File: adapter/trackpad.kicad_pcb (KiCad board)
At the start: 2 copper layers, 41.9 x 19.7 mm, 15 parts, among them J1 J1, U1 Elite-C-nf, U2 ProMicro, U3 U3, U4 NCP1117-2.85_SOT223

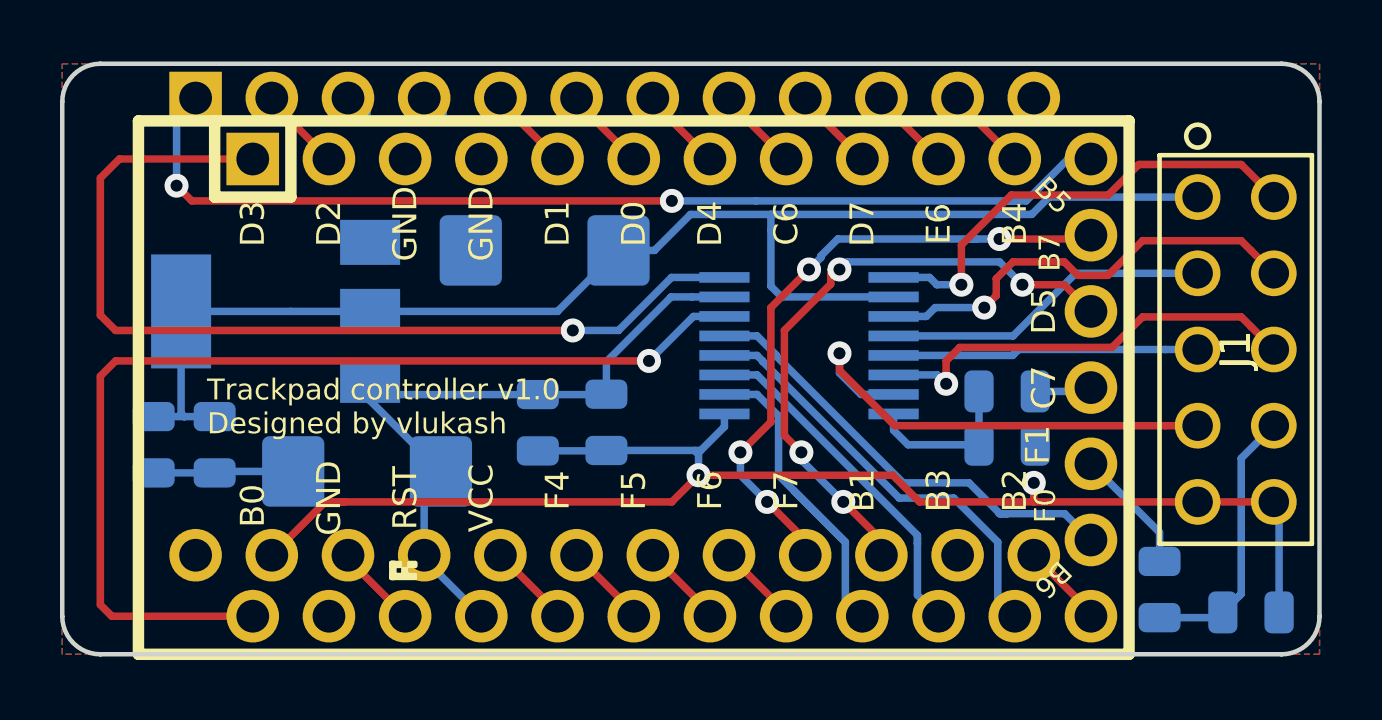
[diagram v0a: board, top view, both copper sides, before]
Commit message: Update PCB length so it doesn't block USB-C connector.
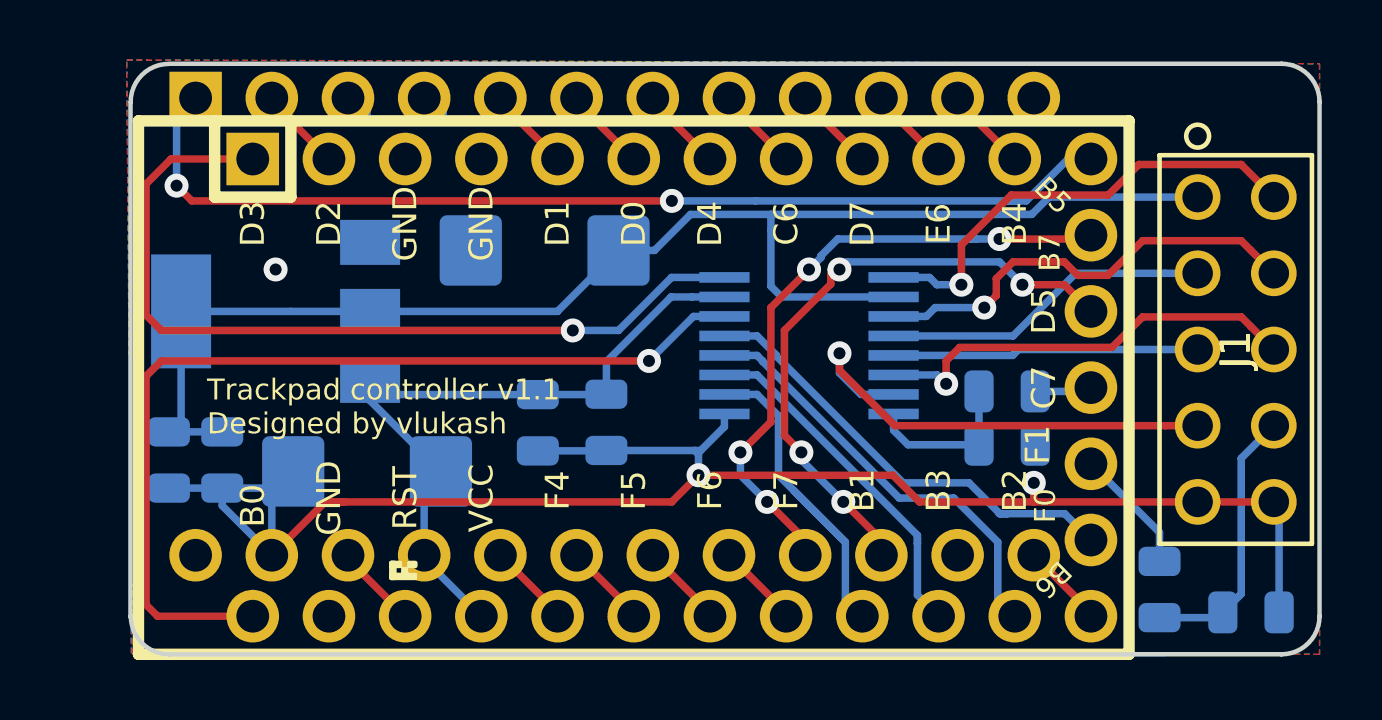
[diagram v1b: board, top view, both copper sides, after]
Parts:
- moved C5 0.72 mm to (98.8, 83.1)
- moved C6 0.57 mm to (100.6, 83.1)
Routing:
- net GND: track 55.8 -> 61.5 mm, vias 2 -> 3
- net TP_MOTION: track 31.7 -> 28.5 mm
- net TP_CS: track 35.9 -> 32.9 mm
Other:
- board size 41.9 x 19.7 mm -> 39.6 x 19.7 mm
- board text added: "Trackpad controller v1.1 Designed by vlukash"
- board text removed: "Trackpad controller v1.0 Designed by vlukash"
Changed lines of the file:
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@@
     (thickness 1.6)
     (drawings 9)
-    (tracks 268)
+    (tracks 272)
     (zones 0)
     (modules 15)
@@
     (title "Adapter PCB")
     (date 2019-01-16)
-    (rev 1.0)
+    (rev 1.1)
     (company vlukash)
   )
@@
     (42 Eco1.User user hide)
     (43 Eco2.User user hide)
-    (44 Edge.Cuts user hide)
+    (44 Edge.Cuts user)
     (45 Margin user hide)
     (46 B.CrtYd user hide)
@@
     (pcbplotparams
       (layerselection 0x010fc_ffffffff)
-      (usegerberextensions false)
+      (usegerberextensions true)
       (usegerberattributes false)
       (usegerberadvancedattributes false)
@@
       (drillshape 0)
       (scaleselection 1)
-      (outputdirectory "../plot/"))
+      (outputdirectory "../plot1/"))
   )
   (net 0 "")
@@
   )
   (module Capacitor_SMD:C_0805_2012Metric (layer B.Cu)
-    (at 98.298 82.55 270)
+    (at 98.806 83.058 270)
     (descr "Capacitor SMD 0805 (2012 Metric), square (rectangular) end terminal, IPC_7351 nominal, (Body size source: https://docs.google.com/spreadsheets/d/1BsfQQcO9C6DZCsRaXUlFlo91Tg2WpOkGARC1WS5S8t0/edit?usp=sharing), generated with kicad-footprint-generator")
     (tags capacitor)
@@
   )
   (module Capacitor_SMD:C_0805_2012Metric (layer B.Cu)
-    (at 100.33 82.55 270)
+    (at 100.584 83.058 270)
     (descr "Capacitor SMD 0805 (2012 Metric), square (rectangular) end terminal, IPC_7351 nominal, (Body size source: https://docs.google.com/spreadsheets/d/1BsfQQcO9C6DZCsRaXUlFlo91Tg2WpOkGARC1WS5S8t0/edit?usp=sharing), generated with kicad-footprint-generator")
     (tags capacitor)
@@
     )
   )
-  (gr_text "Trackpad controller v1.0\nDesigned by vlukash" (at 100.076 81.28) (layer F.SilkS)
+  (gr_text "Trackpad controller v1.1\nDesigned by vlukash" (at 100.076 81.28) (layer F.SilkS)
     (effects (font (size 0.7 0.7) (thickness 0.175)) (justify left))
   )
   (gr_arc (start 135.89 71.12) (end 137.16 71.12) (angle -90) (layer Edge.Cuts) (width 0.15))
   (gr_arc (start 135.89 88.265) (end 135.89 89.535) (angle -90) (layer Edge.Cuts) (width 0.15))
-  (gr_arc (start 96.52 88.265) (end 95.25 88.265) (angle -90) (layer Edge.Cuts) (width 0.15))
-  (gr_arc (start 96.52 71.12) (end 96.52 69.85) (angle -90) (layer Edge.Cuts) (width 0.15))
-  (gr_line (start 95.25 88.265) (end 95.25 71.12) (layer Edge.Cuts) (width 0.15))
-  (gr_line (start 135.89 89.535) (end 96.52 89.535) (layer Edge.Cuts) (width 0.15))
+  (gr_arc (start 98.806 88.265) (end 97.536 88.265) (angle -90) (layer Edge.Cuts) (width 0.15))
+  (gr_arc (start 98.8 71.125) (end 98.8 69.855) (angle -90) (layer Edge.Cuts) (width 0.15))
+  (gr_line (start 97.525 88.295) (end 97.525 71.15) (layer Edge.Cuts) (width 0.15))
+  (gr_line (start 135.89 89.535) (end 98.82 89.54) (layer Edge.Cuts) (width 0.15))
   (gr_line (start 137.16 71.12) (end 137.16 88.265) (layer Edge.Cuts) (width 0.15))
-  (gr_line (start 96.52 69.85) (end 135.89 69.85) (layer Edge.Cuts) (width 0.15))
+  (gr_line (start 98.83 69.85) (end 135.89 69.85) (layer Edge.Cuts) (width 0.15))
   (segment (start 107.95 71.755) (end 107.95 70.993) (width 0.25) (layer B.Cu) (net 1))
   (segment (start 107.95 70.993) (end 106.710725 70.993) (width 0.25) (layer B.Cu) (net 1))
   (segment (start 105.41 71.755) (end 105.41 70.993) (width 0.25) (layer B.Cu) (net 1))
   (segment (start 105.016299 71.386701) (end 105.41 70.993) (width 0.25) (layer B.Cu) (net 1))
-  (segment (start 100.3785 83.439) (end 100.33 83.4875) (width 0.25) (layer B.Cu) (net 1))
-  (segment (start 102.9475 83.439) (end 100.3785 83.439) (width 0.25) (layer B.Cu) (net 1))
-  (segment (start 100.33 83.4875) (end 98.298 83.4875) (width 0.25) (layer B.Cu) (net 1))
   (segment (start 104.013 84.455) (end 102.235 86.233) (width 0.25) (layer F.Cu) (net 1))
   (segment (start 104.648 84.455) (end 104.013 84.455) (width 0.25) (layer F.Cu) (net 1))
@@
   (segment (start 116.332 82.740969) (end 116.53243 82.740969) (width 0.25) (layer B.Cu) (net 1))
   (segment (start 113.388145 82.740969) (end 116.332 82.740969) (width 0.25) (layer B.Cu) (net 1))
+  (segment (start 100.584 83.9955) (end 98.806 83.9955) (width 0.25) (layer B.Cu) (net 1))
+  (segment (start 102.391 83.9955) (end 102.9475 83.439) (width 0.25) (layer B.Cu) (net 1))
+  (segment (start 100.584 83.9955) (end 102.391 83.9955) (width 0.25) (layer B.Cu) (net 1))
+  (segment (start 100.584 84.582) (end 100.584 83.9955) (width 0.25) (layer B.Cu) (net 1))
+  (segment (start 102.235 86.233) (end 100.584 84.582) (width 0.25) (layer B.Cu) (net 1))
+  (segment (start 102.235 84.1515) (end 102.9475 83.439) (width 0.25) (layer B.Cu) (net 1))
+  (segment (start 102.235 86.233) (end 102.235 84.1515) (width 0.25) (layer B.Cu) (net 1))
+  (via (at 102.362 76.708) (size 0.8) (drill 0.4) (layers F.Cu B.Cu) (net 1))
   (segment (start 107.315 86.36) (end 107.315 86.233) (width 0.25) (layer B.Cu) (net 2))
   (segment (start 109.22 88.265) (end 107.315 86.36) (width 0.25) (layer B.Cu) (net 2))
@@
   (segment (start 102.87 78.105) (end 99.212 78.105) (width 0.25) (layer B.Cu) (net 3))
   (segment (start 102.87 78.105) (end 105.512 78.105) (width 0.25) (layer B.Cu) (net 3))
-  (segment (start 99.212 81.5105) (end 99.212 78.105) (width 0.25) (layer B.Cu) (net 3))
-  (segment (start 99.314 81.6125) (end 99.212 81.5105) (width 0.25) (layer B.Cu) (net 3))
-  (segment (start 99.314 81.6125) (end 98.298 81.6125) (width 0.25) (layer B.Cu) (net 3))
-  (segment (start 100.33 81.6125) (end 99.314 81.6125) (width 0.25) (layer B.Cu) (net 3))
   (segment (start 111.76 78.105) (end 113.792 76.073) (width 0.25) (layer B.Cu) (net 3))
   (segment (start 105.512 78.105) (end 111.76 78.105) (width 0.25) (layer B.Cu) (net 3))
@@
   (segment (start 127.567326 74.87201) (end 118.872 74.87201) (width 0.25) (layer B.Cu) (net 3))
   (segment (start 118.872 74.87201) (end 116.192992 74.87201) (width 0.25) (layer B.Cu) (net 3))
+  (segment (start 100.584 82.1205) (end 98.806 82.1205) (width 0.25) (layer B.Cu) (net 3))
+  (segment (start 99.212 81.7145) (end 98.806 82.1205) (width 0.25) (layer B.Cu) (net 3))
+  (segment (start 99.212 78.105) (end 99.212 81.7145) (width 0.25) (layer B.Cu) (net 3))
   (via (at 125.222 77.216) (size 0.8) (drill 0.4) (layers F.Cu B.Cu) (net 4))
   (segment (start 125.222 75.888998) (end 125.222 76.650315) (width 0.25) (layer F.Cu) (net 4))
@@
   (segment (start 101.980926 88.265) (end 101.6 88.265) (width 0.25) (layer F.Cu) (net 16))
   (segment (start 115.020999 79.543001) (end 114.808 79.756) (width 0.25) (layer B.Cu) (net 16))
-  (segment (start 114.808 79.756) (end 97.028 79.756) (width 0.25) (layer F.Cu) (net 16))
-  (segment (start 97.028 79.756) (end 96.52 80.264) (width 0.25) (layer F.Cu) (net 16))
-  (segment (start 96.52 80.264) (end 96.52 87.884) (width 0.25) (layer F.Cu) (net 16))
-  (segment (start 96.901 88.265) (end 101.6 88.265) (width 0.25) (layer F.Cu) (net 16))
-  (segment (start 96.52 87.884) (end 96.901 88.265) (width 0.25) (layer F.Cu) (net 16))
+  (segment (start 98.044 80.264) (end 98.044 87.884) (width 0.25) (layer F.Cu) (net 16))
   (segment (start 116.290999 78.273001) (end 117.3226 78.273001) (width 0.25) (layer B.Cu) (net 16))
   (segment (start 114.808 79.756) (end 116.290999 78.273001) (width 0.25) (layer B.Cu) (net 16))
+  (segment (start 98.425 88.265) (end 101.6 88.265) (width 0.25) (layer F.Cu) (net 16))
+  (segment (start 98.044 87.884) (end 98.425 88.265) (width 0.25) (layer F.Cu) (net 16))
+  (segment (start 98.552 79.756) (end 98.044 80.264) (width 0.25) (layer F.Cu) (net 16))
+  (segment (start 114.808 79.756) (end 98.552 79.756) (width 0.25) (layer F.Cu) (net 16))
   (via (at 115.57 74.422) (size 0.8) (drill 0.4) (layers F.Cu B.Cu) (net 17))
   (via (at 99.06 73.914) (size 0.8) (drill 0.4) (layers F.Cu B.Cu) (net 17))
@@
   (segment (start 104.14 73.025) (end 102.235 71.12) (width 0.25) (layer F.Cu) (net 34))
   (via (at 112.268 78.74) (size 0.8) (drill 0.4) (layers F.Cu B.Cu) (net 35))
-  (segment (start 97.155 73.025) (end 101.6 73.025) (width 0.25) (layer F.Cu) (net 35))
-  (segment (start 96.52 78.232) (end 96.52 73.66) (width 0.25) (layer F.Cu) (net 35))
-  (segment (start 112.268 78.74) (end 97.028 78.74) (width 0.25) (layer F.Cu) (net 35))
-  (segment (start 96.52 73.66) (end 97.155 73.025) (width 0.25) (layer F.Cu) (net 35))
-  (segment (start 97.028 78.74) (end 96.52 78.232) (width 0.25) (layer F.Cu) (net 35))
   (segment (start 115.558999 76.973001) (end 117.3226 76.973001) (width 0.25) (layer B.Cu) (net 35))
   (segment (start 112.268 78.74) (end 113.792 78.74) (width 0.25) (layer B.Cu) (net 35))
   (segment (start 113.792 78.74) (end 115.558999 76.973001) (width 0.25) (layer B.Cu) (net 35))
+  (segment (start 112.268 78.74) (end 98.552 78.74) (width 0.25) (layer F.Cu) (net 35))
+  (segment (start 98.552 78.74) (end 98.044 78.232) (width 0.25) (layer F.Cu) (net 35))
+  (segment (start 98.875998 73.025) (end 98.044 73.856998) (width 0.25) (layer F.Cu) (net 35))
+  (segment (start 98.044 73.856998) (end 98.044 78.232) (width 0.25) (layer F.Cu) (net 35))
+  (segment (start 101.6 73.025) (end 98.875998 73.025) (width 0.25) (layer F.Cu) (net 35))
   (segment (start 133.761 88.3135) (end 133.9365 88.138) (width 0.25) (layer B.Cu) (net 39))
   (segment (start 131.826 88.3135) (end 133.761 88.3135) (width 0.25) (layer B.Cu) (net 39))
@@
     (polygon
       (pts
-        (xy 95.25 69.85) (xy 137.16 69.85) (xy 137.16 89.535) (xy 95.25 89.535)
+        (xy 97.4 69.725) (xy 137.16 69.85) (xy 137.16 89.535) (xy 97.575 89.525)
       )
     )
@@
     (polygon
       (pts
-        (xy 137.16 69.85) (xy 137.16 89.535) (xy 95.25 89.535) (xy 95.25 69.85)
+        (xy 137.16 69.85) (xy 137.16 89.535) (xy 97.55 89.5) (xy 97.4 69.725)
       )
     )
